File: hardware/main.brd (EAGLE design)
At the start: 39.4 x 66.7 mm, 8 parts, among them X1 JACK, X2 POWER

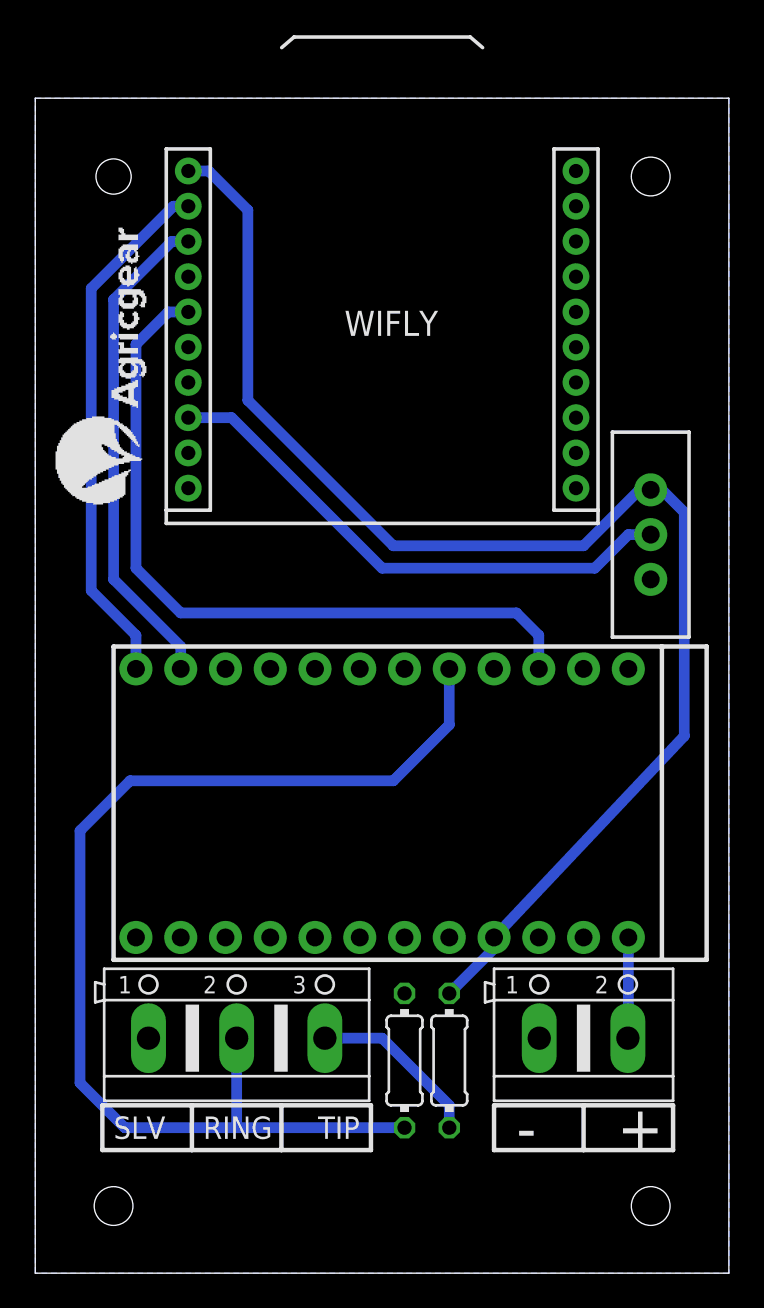
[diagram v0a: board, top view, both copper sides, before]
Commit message: Añadidos cambios sobre el hardware y el firmware del prototipo final.
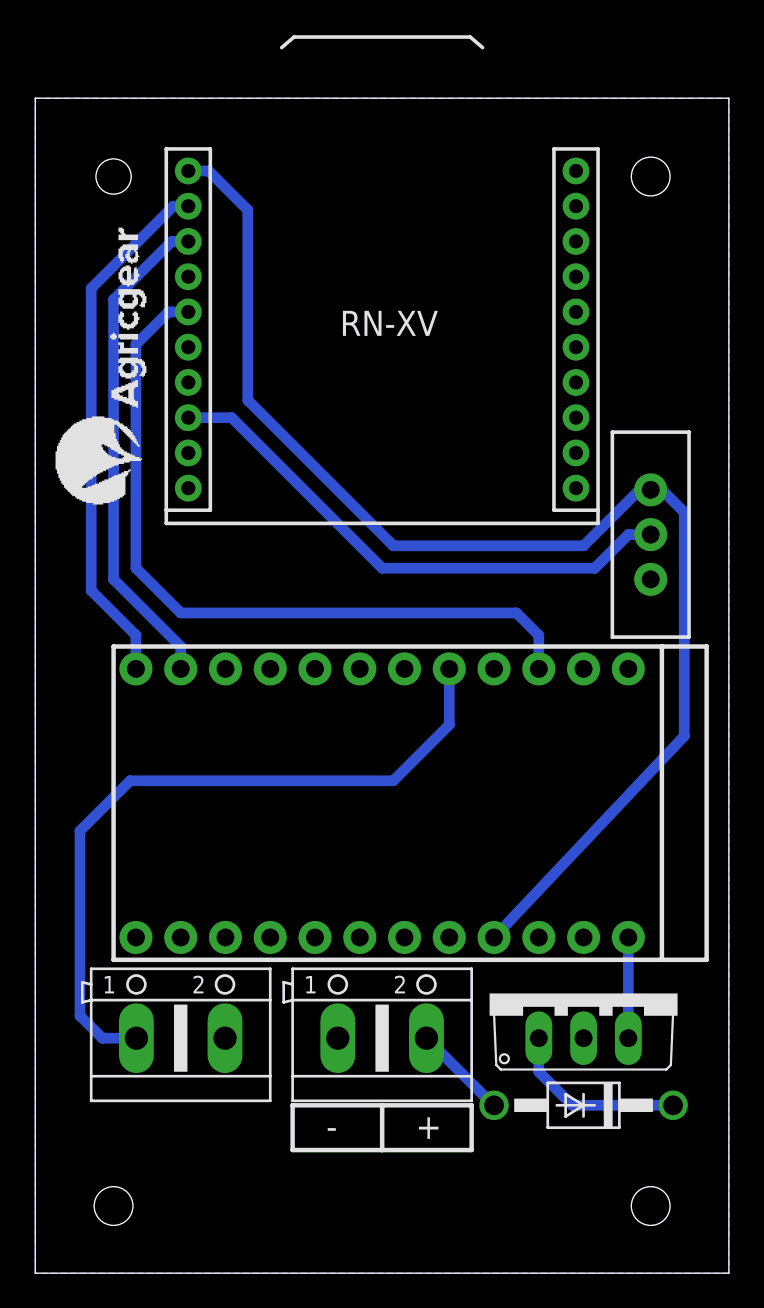
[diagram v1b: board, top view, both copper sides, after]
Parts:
- removed R1: 150, resistor:0204/7
- removed R2: 10K, resistor:0204/7
- removed X1: JACK, con-ptr500:AK500/3
- added D1: 1N4004, diode:DO41-10
- added IC1: 7805, linear:TO220V
- added X3: SWITCH, con-ptr500:AK500/2
- moved X2 11.4 mm to (19.7, 13.3)
- renumbered WIFLY to RN-XV
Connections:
- new net N$2: D1.C, IC1.1
- net GND: now also IC1.2, X3.2; no longer R2.1, X1.1
- net N$1: now also D1.A, X2.2; no longer R1.1, X1.3
- net RAW: now also IC1.3; no longer X2.2
- net SWITCH: now also X3.1; no longer R2.2, X1.2
- net VCC: no longer R1.2
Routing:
- net SWITCH: track 65.5 -> 40.8 mm
- net N$2: track 0.00 -> 10.3 mm
- net N$1: track 9.91 -> 5.41 mm
- net VCC: track 77.8 -> 74.2 mm
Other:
- board text removed: "RING"
- board text removed: "SLV"
- board text removed: "TIP"
